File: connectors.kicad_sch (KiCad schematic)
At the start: 18 parts, among them J5 Grove, J6 Grove, J7 PinSocket_1x06, J8 Conn_01x06, U10 H5VU25UC, U11 H5VU25UC, U8 H5VU25UC, U9 H5VU25UC

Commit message: Rev.2 (260322)
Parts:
- removed C33: 100n, Capacitor_SMD:C_0603_1608Metric, symbol Device:C
- removed D6, D9: H5VHD3BC, Diode_SMD:D_SOD-323, symbol Device:D_TVS
- removed D7, D8: H3V3SD3B, Diode_SMD:D_SOD-323, symbol Device:D_TVS
- removed J6: Grove, Connector:NS-Tech_Grove_1x04_P2mm_Vertical, symbol Connector_Generic:Conn_01x04
- removed J8: Conn_01x06, Harucom_Board:RaspberryPi_Pico_Debug_Probe, symbol Connector_Generic:Conn_01x06
- removed U10, U11, U8, U9: H5VU25UC, Harucom_Board:Diodes_DFN2510-10L-10_1x2.5mm_P0.5mm, symbol Hakodate_Board:H5VU25UC
- added J6: Conn_01x05, Connector_PinSocket_2.54mm:PinSocket_1x05_P2.54mm_Vertical, symbol Connector_Generic:Conn_01x05
- added J7: Conn_01x04, Connector_PinHeader_2.54mm:PinHeader_1x04_P2.54mm_Vertical, symbol Connector_Generic:Conn_01x04
- added R46, R47, R52, R53: 100, Resistor_SMD:R_0603_1608Metric, symbol Device:R
- added R48, R49, R50, R51, R55, R56, R57, R58: 22, Resistor_SMD:R_0603_1608Metric, symbol Device:R
- added R54: 10k, Resistor_SMD:R_0603_1608Metric, symbol Device:R
- C30, C31, C32: LCSC (none) -> C14663
- R44, R45: LCSC (none) -> C25900
- renumbered J7 to J8
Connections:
- net +3V3: now also J7.2 (Pin_2), R54.1
- net +5V: now also J5.3 (Pin_3); no longer J5.2 (Pin_2)
- net GND: now also J5.4 (Pin_4), J6.1 (Pin_1), J7.1 (Pin_1); no longer J5.1 (Pin_1)
- net SPI_CS: now also R54.2, R55.1; no longer J8.3 (Pin_3)
- net SPI_RX: now also R56.1; no longer J8.4 (Pin_4)
- net SPI_SCK: now also R58.1; no longer J8.6 (Pin_6)
- net SPI_TX: now also R57.1; no longer J8.5 (Pin_5)
- net SWCLK: now also R48.1
- net SWDIO: now also R49.2
- net UART0_RX: now also R50.1
- net UART0_TX: now also R51.1
- net I2C_SDA renamed I2C0_SDA
- net I2C0_SDA: now also R47.1; no longer J5.3 (Pin_3)
- net I2C_SDL renamed I2C0_SCL
- net I2C0_SCL: now also R46.1; no longer J5.4 (Pin_4)
- new net: J6.5 (Pin_5), R51.2
- new net: J7.4 (Pin_4), R53.2
- new net: J6.2 (Pin_2), R48.2
- new net: J7.3 (Pin_3), R52.2
- new net: J5.1 (Pin_1), R46.2
- new net: J8.6 (Pin_6), R58.2
- new net: J8.3 (Pin_3), R55.2
- new net: J8.4 (Pin_4), R56.2
- new net: J8.5 (Pin_5), R57.2
- new net: J5.2 (Pin_2), R47.2
- new net: J6.3 (Pin_3), R49.1
- new net: J6.4 (Pin_4), R50.2
- new net I2C1_SCL: R52.1
- new net I2C1_SDA: R53.1
- no-connect marks 8 -> 0
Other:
- note added: "I2C0"
- note added: "I2C1"
- note removed: "I2C"
- note removed: "UART/I2C/ADC (3.3V)"
- moved on the sheet: C30, C31, C32, J5, J8, R44, R45

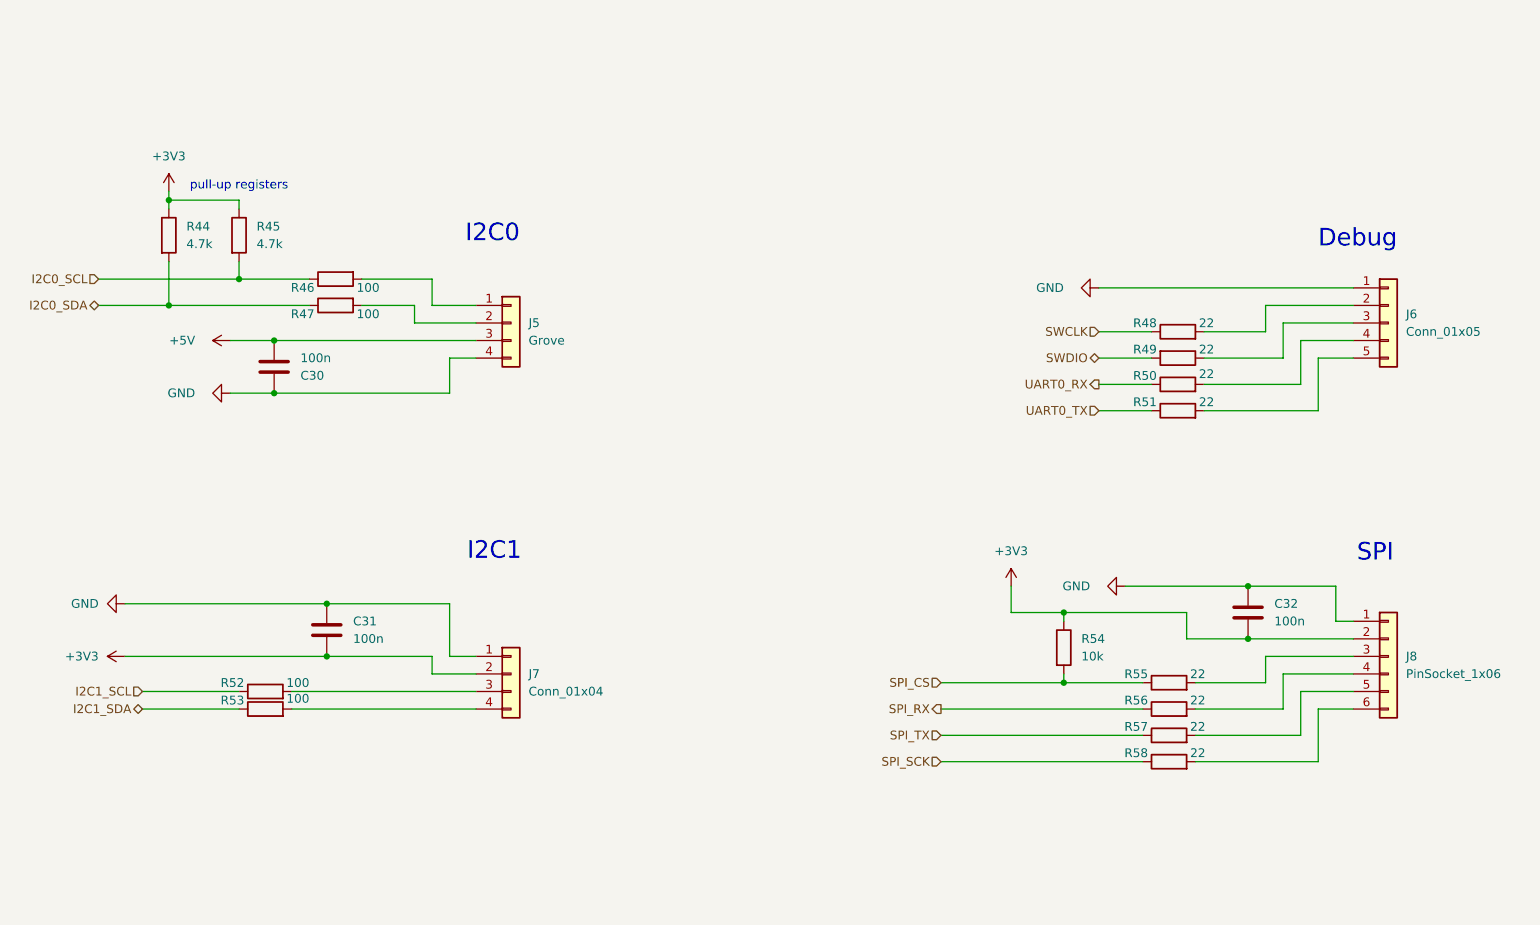
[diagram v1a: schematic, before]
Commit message: Rev. 2B: Change PSRAM package from SOP-8 to USON-8L.
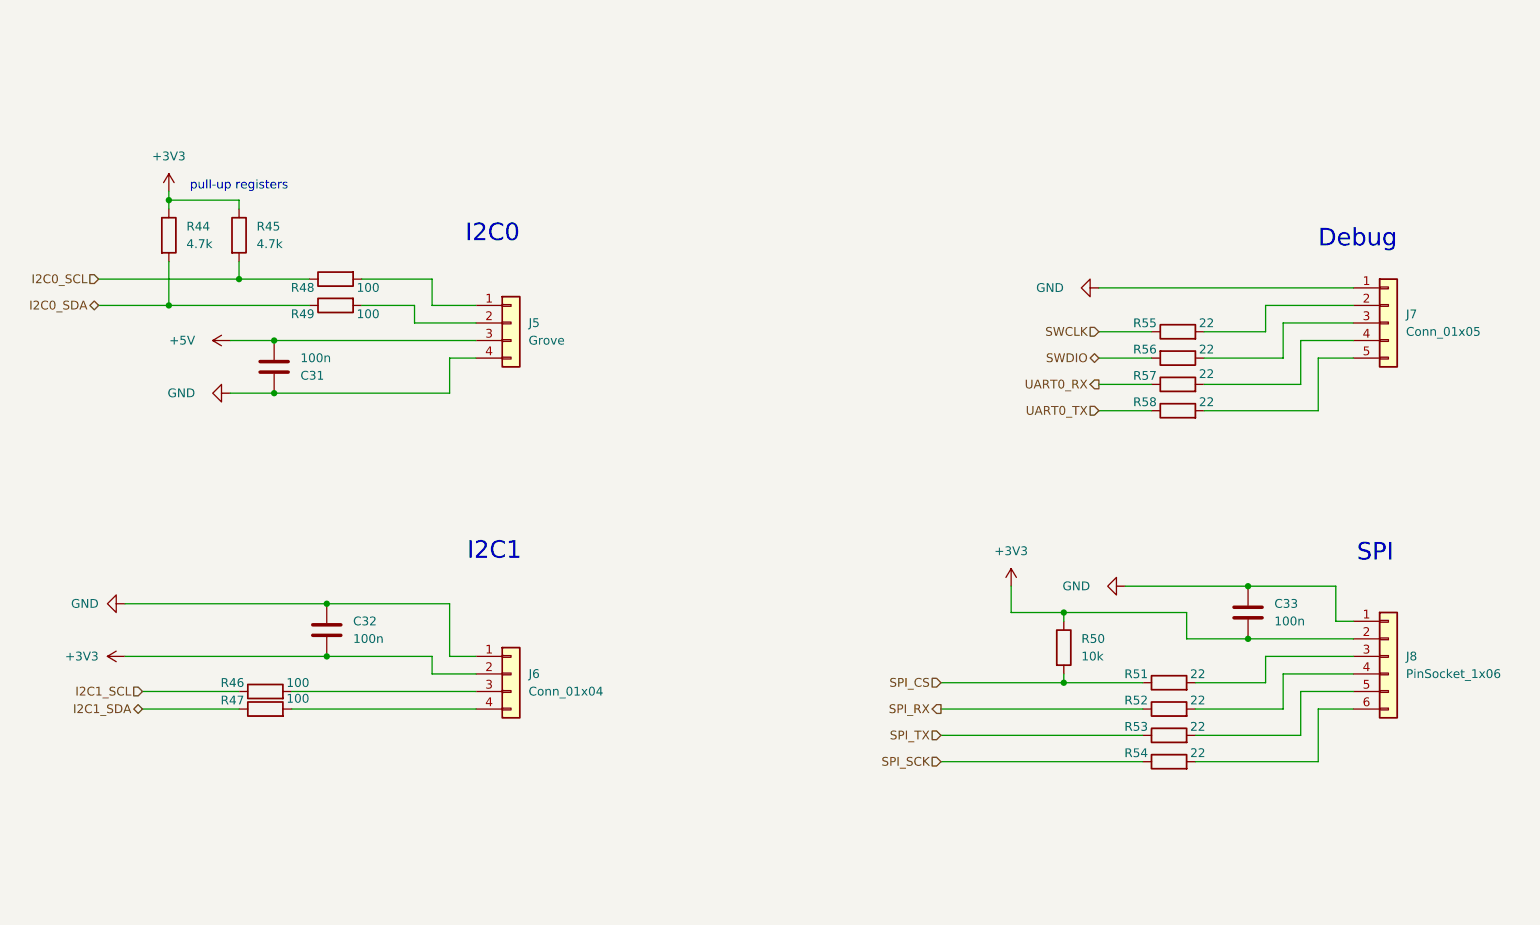
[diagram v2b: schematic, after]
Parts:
- renumbered C30 to C31, C31 to C32, C32 to C33, J7 to J6, J6 to J7, R52 to R46, R53 to R47, R46 to R48, R47 to R49, R54 to R50, R55 to R51, R56 to R52, R57 to R53, R58 to R54, R48 to R55, R49 to R56, R50 to R57, R51 to R58
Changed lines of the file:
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@@
 	(title_block
 		(title "Harucom-board")
-		(date "2026-03-22")
-		(rev "2")
+		(date "2026-03-23")
+		(rev "2B")
 		(comment 1 "https://github.com/harukasan/harucom-board/")
 		(comment 2 "SPDX-License-Identifier: CERN-OHL-P-2.0")
@@
 		(on_board yes)
 		(dnp no)
-		(property "Reference" "R51"
+		(property "Reference" "R58"
 			(at 193.802 82.042 90)
 			(effects
@@
 			(project ""
 				(path "/0cb5192e-ac62-478f-bacb-beb1b9be1a5b/ebbffcac-f15c-4d26-8daa-0fcadec9c80c"
-					(reference "R51")
+					(reference "R58")
 					(unit 1)
 				)
@@
 		(dnp no)
 		(fields_autoplaced yes)
-		(property "Reference" "#PWR064"
+		(property "Reference" "#PWR063"
 			(at 172.72 111.76 0)
 			(effects
@@
 			(project "hakodate-board"
 				(path "/0cb5192e-ac62-478f-bacb-beb1b9be1a5b/ebbffcac-f15c-4d26-8daa-0fcadec9c80c"
-					(reference "#PWR064")
+					(reference "#PWR063")
 					(unit 1)
 				)
@@
 		(dnp no)
 		(fields_autoplaced yes)
-		(property "Reference" "C32"
+		(property "Reference" "C33"
 			(at 210.82 110.4899 0)
 			(effects
@@
 			(project "hakodate-board"
 				(path "/0cb5192e-ac62-478f-bacb-beb1b9be1a5b/ebbffcac-f15c-4d26-8daa-0fcadec9c80c"
-					(reference "C32")
+					(reference "C33")
 					(unit 1)
 				)
@@
 		(on_board yes)
 		(dnp no)
-		(property "Reference" "#PWR060"
+		(property "Reference" "#PWR062"
 			(at 53.34 80.01 0)
 			(effects
@@
 			(project ""
 				(path "/0cb5192e-ac62-478f-bacb-beb1b9be1a5b/ebbffcac-f15c-4d26-8daa-0fcadec9c80c"
-					(reference "#PWR060")
+					(reference "#PWR062")
 					(unit 1)
 				)
@@
 		(on_board yes)
 		(dnp no)
-		(property "Reference" "#PWR059"
+		(property "Reference" "#PWR061"
 			(at 63.5 72.39 0)
 			(effects
@@
 			(project ""
 				(path "/0cb5192e-ac62-478f-bacb-beb1b9be1a5b/ebbffcac-f15c-4d26-8daa-0fcadec9c80c"
-					(reference "#PWR059")
+					(reference "#PWR061")
 					(unit 1)
 				)
@@
 		(on_board yes)
 		(dnp no)
-		(property "Reference" "R53"
+		(property "Reference" "R47"
 			(at 61.722 125.222 90)
 			(effects
@@
 			(project "harucom-board"
 				(path "/0cb5192e-ac62-478f-bacb-beb1b9be1a5b/ebbffcac-f15c-4d26-8daa-0fcadec9c80c"
-					(reference "R53")
+					(reference "R47")
 					(unit 1)
 				)
@@
 		(dnp no)
 		(fields_autoplaced yes)
-		(property "Reference" "R54"
+		(property "Reference" "R50"
 			(at 182.88 115.5699 0)
 			(effects
@@
 			(project ""
 				(path "/0cb5192e-ac62-478f-bacb-beb1b9be1a5b/ebbffcac-f15c-4d26-8daa-0fcadec9c80c"
-					(reference "R54")
+					(reference "R50")
 					(unit 1)
 				)
@@
 		(on_board yes)
 		(dnp no)
-		(property "Reference" "R48"
+		(property "Reference" "R55"
 			(at 193.802 70.612 90)
 			(effects
@@
 			(project ""
 				(path "/0cb5192e-ac62-478f-bacb-beb1b9be1a5b/ebbffcac-f15c-4d26-8daa-0fcadec9c80c"
-					(reference "R48")
+					(reference "R55")
 					(unit 1)
 				)
@@
 		(on_board yes)
 		(dnp no)
-		(property "Reference" "R52"
+		(property "Reference" "R46"
 			(at 61.722 122.682 90)
 			(effects
@@
 			(project "harucom-board"
 				(path "/0cb5192e-ac62-478f-bacb-beb1b9be1a5b/ebbffcac-f15c-4d26-8daa-0fcadec9c80c"
-					(reference "R52")
+					(reference "R46")
 					(unit 1)
 				)
@@
 		(on_board yes)
 		(dnp no)
-		(property "Reference" "R46"
+		(property "Reference" "R48"
 			(at 71.882 64.008 90)
 			(effects
@@
 			(project ""
 				(path "/0cb5192e-ac62-478f-bacb-beb1b9be1a5b/ebbffcac-f15c-4d26-8daa-0fcadec9c80c"
-					(reference "R46")
+					(reference "R48")
 					(unit 1)
 				)
@@
 		(dnp no)
 		(fields_autoplaced yes)
-		(property "Reference" "#PWR063"
+		(property "Reference" "#PWR059"
 			(at 48.26 118.11 0)
 			(effects
@@
 			(project "hakodate-board"
 				(path "/0cb5192e-ac62-478f-bacb-beb1b9be1a5b/ebbffcac-f15c-4d26-8daa-0fcadec9c80c"
-					(reference "#PWR063")
+					(reference "#PWR059")
 					(unit 1)
 				)
@@
 		(on_board yes)
 		(dnp no)
-		(property "Reference" "R58"
+		(property "Reference" "R54"
 			(at 192.532 132.842 90)
 			(effects
@@
 			(project "harucom-board"
 				(path "/0cb5192e-ac62-478f-bacb-beb1b9be1a5b/ebbffcac-f15c-4d26-8daa-0fcadec9c80c"
-					(reference "R58")
+					(reference "R54")
 					(unit 1)
 				)
@@
 		(on_board yes)
 		(dnp no)
-		(property "Reference" "R55"
+		(property "Reference" "R51"
 			(at 192.532 121.412 90)
 			(effects
@@
 			(project "harucom-board"
 				(path "/0cb5192e-ac62-478f-bacb-beb1b9be1a5b/ebbffcac-f15c-4d26-8daa-0fcadec9c80c"
-					(reference "R55")
+					(reference "R51")
 					(unit 1)
 				)
@@
 		(dnp no)
 		(fields_autoplaced yes)
-		(property "Reference" "C30"
+		(property "Reference" "C31"
 			(at 69.85 77.4701 0)
 			(effects
@@
 			(project ""
 				(path "/0cb5192e-ac62-478f-bacb-beb1b9be1a5b/ebbffcac-f15c-4d26-8daa-0fcadec9c80c"
-					(reference "C30")
+					(reference "C31")
 					(unit 1)
 				)
@@
 		(on_board yes)
 		(dnp no)
-		(property "Reference" "R57"
+		(property "Reference" "R53"
 			(at 192.532 129.032 90)
 			(effects
@@
 			(project "harucom-board"
 				(path "/0cb5192e-ac62-478f-bacb-beb1b9be1a5b/ebbffcac-f15c-4d26-8daa-0fcadec9c80c"
-					(reference "R57")
+					(reference "R53")
 					(unit 1)
 				)
@@
 		(dnp no)
 		(fields_autoplaced yes)
-		(property "Reference" "#PWR058"
+		(property "Reference" "#PWR060"
 			(at 50.8 54.61 0)
 			(effects
@@
 			(project ""
 				(path "/0cb5192e-ac62-478f-bacb-beb1b9be1a5b/ebbffcac-f15c-4d26-8daa-0fcadec9c80c"
-					(reference "#PWR058")
+					(reference "#PWR060")
 					(unit 1)
 				)
@@
 		(on_board yes)
 		(dnp no)
-		(property "Reference" "R47"
+		(property "Reference" "R49"
 			(at 71.882 67.818 90)
 			(effects
@@
 			(project ""
 				(path "/0cb5192e-ac62-478f-bacb-beb1b9be1a5b/ebbffcac-f15c-4d26-8daa-0fcadec9c80c"
-					(reference "R47")
+					(reference "R49")
 					(unit 1)
 				)
@@
 		(dnp no)
 		(fields_autoplaced yes)
-		(property "Reference" "#PWR062"
+		(property "Reference" "#PWR058"
 			(at 38.1 110.49 0)
 			(effects
@@
 			(project "hakodate-board"
 				(path "/0cb5192e-ac62-478f-bacb-beb1b9be1a5b/ebbffcac-f15c-4d26-8daa-0fcadec9c80c"
-					(reference "#PWR062")
+					(reference "#PWR058")
 					(unit 1)
 				)
@@
 		(dnp no)
 		(fields_autoplaced yes)
-		(property "Reference" "J7"
+		(property "Reference" "J6"
 			(at 102.87 120.6499 0)
 			(effects
@@
 			(project ""
 				(path "/0cb5192e-ac62-478f-bacb-beb1b9be1a5b/ebbffcac-f15c-4d26-8daa-0fcadec9c80c"
-					(reference "J7")
+					(reference "J6")
 					(unit 1)
 				)
@@
 		(on_board yes)
 		(dnp no)
-		(property "Reference" "R49"
+		(property "Reference" "R56"
 			(at 193.802 74.422 90)
 			(effects
@@
 			(project ""
 				(path "/0cb5192e-ac62-478f-bacb-beb1b9be1a5b/ebbffcac-f15c-4d26-8daa-0fcadec9c80c"
-					(reference "R49")
+					(reference "R56")
 					(unit 1)
 				)
@@
 		(on_board yes)
 		(dnp no)
-		(property "Reference" "#PWR061"
+		(property "Reference" "#PWR064"
 			(at 179.07 64.77 0)
 			(effects
@@
 			(project "hakodate-board"
 				(path "/0cb5192e-ac62-478f-bacb-beb1b9be1a5b/ebbffcac-f15c-4d26-8daa-0fcadec9c80c"
-					(reference "#PWR061")
+					(reference "#PWR064")
 					(unit 1)
 				)
@@
 		(on_board yes)
 		(dnp no)
-		(property "Reference" "R56"
+		(property "Reference" "R52"
 			(at 192.532 125.222 90)
 			(effects
@@
 			(project "harucom-board"
 				(path "/0cb5192e-ac62-478f-bacb-beb1b9be1a5b/ebbffcac-f15c-4d26-8daa-0fcadec9c80c"
-					(reference "R56")
+					(reference "R52")
 					(unit 1)
 				)
@@
 		(dnp no)
 		(fields_autoplaced yes)
-		(property "Reference" "J6"
+		(property "Reference" "J7"
 			(at 229.87 68.5799 0)
 			(effects
@@
 			(project ""
 				(path "/0cb5192e-ac62-478f-bacb-beb1b9be1a5b/ebbffcac-f15c-4d26-8daa-0fcadec9c80c"
-					(reference "J6")
+					(reference "J7")
 					(unit 1)
 				)
@@
 		(dnp no)
 		(fields_autoplaced yes)
-		(property "Reference" "C31"
+		(property "Reference" "C32"
 			(at 77.47 113.0299 0)
 			(effects
@@
 			(project ""
 				(path "/0cb5192e-ac62-478f-bacb-beb1b9be1a5b/ebbffcac-f15c-4d26-8daa-0fcadec9c80c"
-					(reference "C31")
+					(reference "C32")
 					(unit 1)
 				)
@@
 		(on_board yes)
 		(dnp no)
-		(property "Reference" "R50"
+		(property "Reference" "R57"
 			(at 193.802 78.232 90)
 			(effects
@@
 			(project ""
 				(path "/0cb5192e-ac62-478f-bacb-beb1b9be1a5b/ebbffcac-f15c-4d26-8daa-0fcadec9c80c"
-					(reference "R50")
+					(reference "R57")
 					(unit 1)
 				)
